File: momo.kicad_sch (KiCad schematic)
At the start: 97 parts, among them SW1 MX_SW_HS, SW10 MX_SW_HS, SW11 MX_SW_HS, SW12 MX_SW_HS, SW13 MX_SW_HS, SW14 MX_SW_HS, SW15 MX_SW_HS, SW16 MX_SW_HS, SW17 MX_SW_HS, SW18 MX_SW_HS, SW19 MX_SW_HS, SW2 MX_SW_HS, SW20 MX_SW_HS, SW21 MX_SW_HS, SW22 MX_SW_HS, SW23 MX_SW_HS, SW24 MX_SW_HS, SW25 MX_SW_HS, SW26 MX_SW_HS, SW27 MX_SW_HS, SW28 MX_SW_HS, SW29 MX_SW_HS, SW3 MX_SW_HS, SW30 MX_SW_HS, SW31 MX_SW_HS, SW32 MX_SW_HS, SW33 MX_SW_HS, SW34 MX_SW_HS, SW35 MX_SW_HS, SW36 MX_SW_HS, SW37 MX_SW_HS, SW38 MX_SW_HS, SW39 MX_SW_HS, SW4 MX_SW_HS, SW40 MX_SW_HS, SW41 MX_SW_HS, SW42 MX_SW_HS, SW43 MX_SW_HS, SW44 MX_SW_HS, SW45 MX_SW_HS, SW46 MX_SW_HS, SW47 MX_SW_HS, SW48 MX_SW_HS, SW5 MX_SW_HS, SW6 MX_SW_HS, SW7 MX_SW_HS, SW8 MX_SW_HS, SW9 MX_SW_HS, U1 WeAct-RP2040-Pico

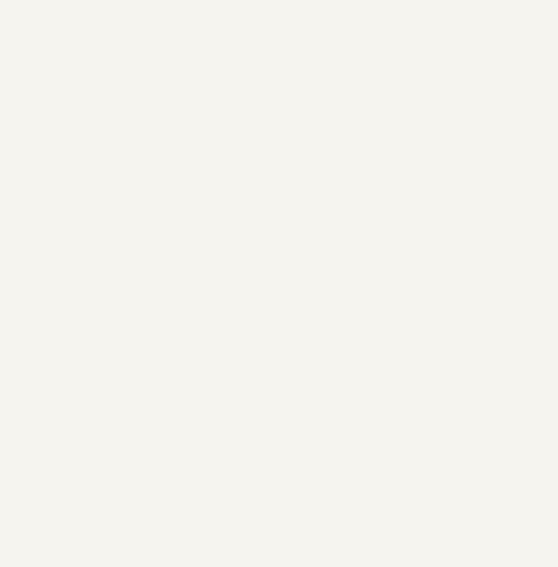
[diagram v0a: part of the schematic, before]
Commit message: Added RGB backlight functionality
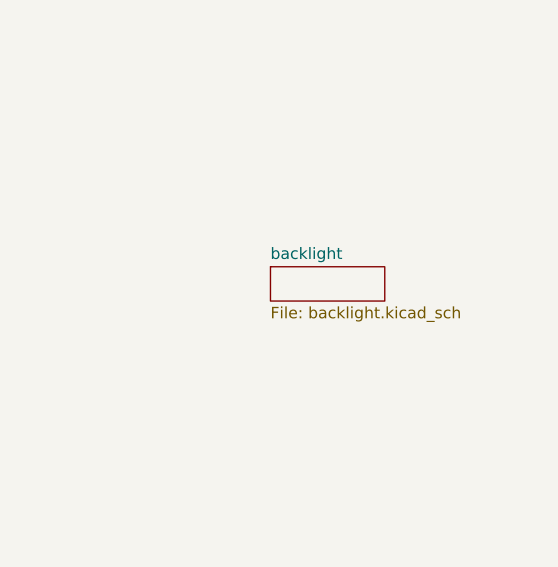
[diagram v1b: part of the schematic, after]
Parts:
- D1, D10, D11, D12, D13, D14, D15, D16, D17, D18, D19, D2, D20, D21, D22, D23, D24, D25, D26, D27, D28, D29, D3, D30, D31, D32, D33, D34, D35, D36, D37, D38, D39, D4, D40, D41, D42, D43, D44, D45, D46, D47, D48, D5, D6, D7, D8, D9: footprint (none) -> keyboard_parts:D_SOD123_axial
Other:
- added sheet backlight (backlight.kicad_sch)

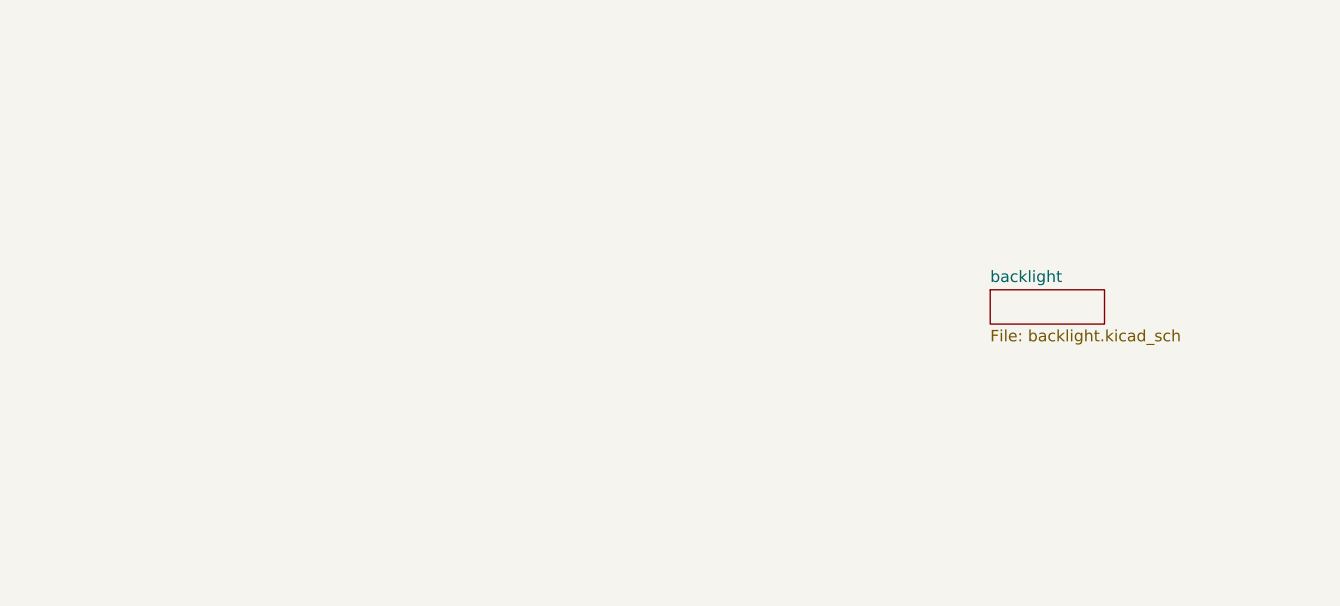
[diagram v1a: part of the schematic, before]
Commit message: Added RGB underglow functionality
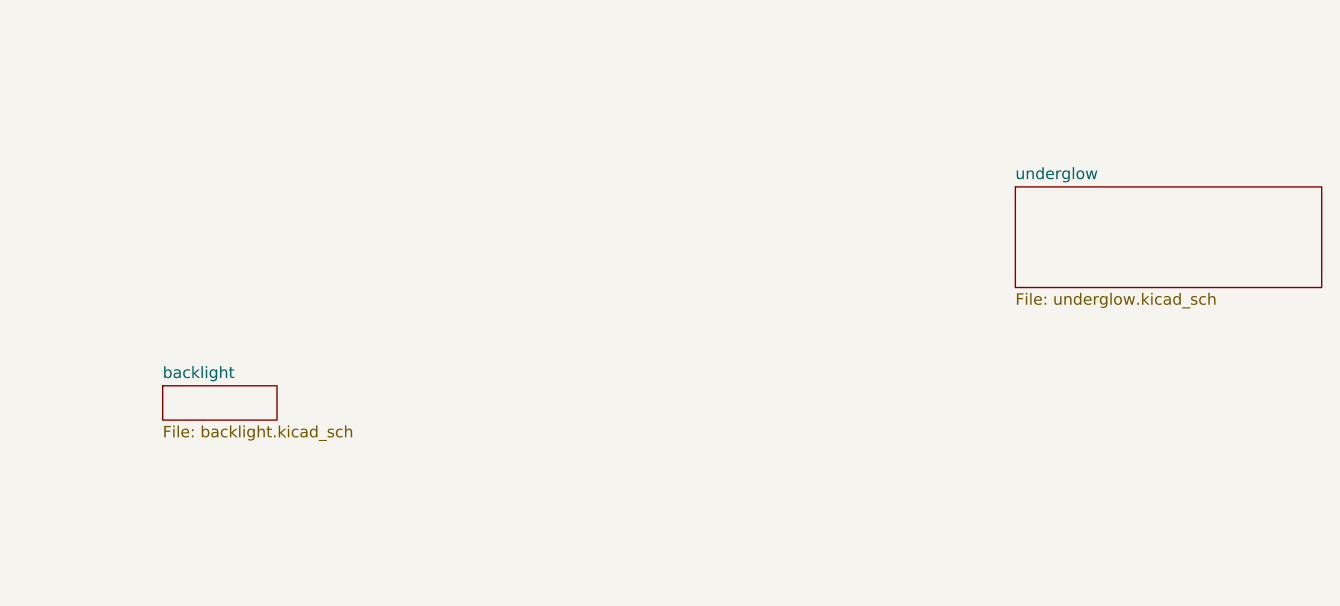
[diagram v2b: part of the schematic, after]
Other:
- added sheet underglow (underglow.kicad_sch)
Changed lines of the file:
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@@
     (pin "9")
   )
-  (sheet (at 311.15 114.3) (size 12.7 3.81) (fields_autoplaced)
+  (sheet (at 219.202 124.968) (size 12.7 3.81) (fields_autoplaced)
     (stroke (width 0.1524) (type solid) (color 0 0 0 0))
     (fill (color 0 0 0 0.0000))
-    (property "Sheet name" "backlight" (id 0) (at 311.15 113.5884 0)
+    (property "Sheet name" "backlight" (id 0) (at 219.202 124.2564 0)
       (effects (font (size 1.27 1.27)) (justify left bottom))
     )
-    (property "Sheet file" "backlight.kicad_sch" (id 1) (at 311.15 118.6946 0)
+    (property "Sheet file" "backlight.kicad_sch" (id 1) (at 219.202 129.3626 0)
+      (effects (font (size 1.27 1.27)) (justify left top))
+    )
+  )
+  (sheet (at 313.944 102.87) (size 34.036 11.176) (fields_autoplaced)
+    (stroke (width 0.1524) (type solid) (color 0 0 0 0))
+    (fill (color 0 0 0 0.0000))
+    (property "Sheet name" "underglow" (id 0) (at 313.944 102.1584 0)
+      (effects (font (size 1.27 1.27)) (justify left bottom))
+    )
+    (property "Sheet file" "underglow.kicad_sch" (id 1) (at 313.944 114.6306 0)
       (effects (font (size 1.27 1.27)) (justify left top))
     )
@@
     (path "/" (page "1"))
     (path "/9d24d119-5b7b-4dd6-a77e-8432ed719570" (page "2"))
+    (path "/e99cffce-74a9-4be0-80a2-98bb8f0554b7" (page "3"))
   )
   (symbol_instances
@@
       (reference "#PWR054") (unit 1) (value "GND") (footprint "")
     )
+    (path "/e99cffce-74a9-4be0-80a2-98bb8f0554b7/1af3a3ca-3065-4f35-8f4b-531eea546ad6"
+      (reference "#PWR?") (unit 1) (value "VCC") (footprint "")
+    )
+    (path "/e99cffce-74a9-4be0-80a2-98bb8f0554b7/255bcbfd-1fd3-4c57-852c-073117da9470"
+      (reference "#PWR?") (unit 1) (value "VCC") (footprint "")
+    )
+    (path "/e99cffce-74a9-4be0-80a2-98bb8f0554b7/286c519f-e218-4927-92ca-c6648bc9f5d4"
+      (reference "#PWR?") (unit 1) (value "GND") (footprint "")
+    )
+    (path "/e99cffce-74a9-4be0-80a2-98bb8f0554b7/33a2550f-d245-4f02-b01e-f1089cd2cb34"
+      (reference "#PWR?") (unit 1) (value "VCC") (footprint "")
+    )
+    (path "/e99cffce-74a9-4be0-80a2-98bb8f0554b7/33e3d1bd-c09b-499f-b8c0-71441a674e76"
+      (reference "#PWR?") (unit 1) (value "VCC") (footprint "")
+    )
+    (path "/e99cffce-74a9-4be0-80a2-98bb8f0554b7/385bfec2-21a7-4a18-8691-a085658c8c89"
+      (reference "#PWR?") (unit 1) (value "VCC") (footprint "")
+    )
+    (path "/e99cffce-74a9-4be0-80a2-98bb8f0554b7/3a7e117d-9009-4a92-9ae7-3cf95631112e"
+      (reference "#PWR?") (unit 1) (value "GND") (footprint "")
+    )
+    (path "/e99cffce-74a9-4be0-80a2-98bb8f0554b7/3c217400-aed6-4acf-baff-9668b9028e4b"
+      (reference "#PWR?") (unit 1) (value "GND") (footprint "")
+    )
+    (path "/e99cffce-74a9-4be0-80a2-98bb8f0554b7/62fb68a9-3c67-4fad-b4d3-634e314d79bf"
+      (reference "#PWR?") (unit 1) (value "GND") (footprint "")
+    )
+    (path "/e99cffce-74a9-4be0-80a2-98bb8f0554b7/69a943d2-1d0b-496f-aca7-fc0dc1ca3e16"
+      (reference "#PWR?") (unit 1) (value "GND") (footprint "")
+    )
+    (path "/e99cffce-74a9-4be0-80a2-98bb8f0554b7/7f8e8ff6-c975-4254-a2c8-bf0f49491244"
+      (reference "#PWR?") (unit 1) (value "GND") (footprint "")
+    )
+    (path "/e99cffce-74a9-4be0-80a2-98bb8f0554b7/8433c9fe-1841-4b4e-be0a-2f042f79798d"
+      (reference "#PWR?") (unit 1) (value "VCC") (footprint "")
+    )
+    (path "/e99cffce-74a9-4be0-80a2-98bb8f0554b7/84b65d91-59f9-435a-bb3c-18beb66e7de1"
+      (reference "#PWR?") (unit 1) (value "GND") (footprint "")
+    )
+    (path "/e99cffce-74a9-4be0-80a2-98bb8f0554b7/85c0819e-bd9a-43dd-8d40-a49c2e72ec3b"
+      (reference "#PWR?") (unit 1) (value "GND") (footprint "")
+    )
+    (path "/e99cffce-74a9-4be0-80a2-98bb8f0554b7/a5c5ebd3-0b2f-4c58-84b9-0acfd348a118"
+      (reference "#PWR?") (unit 1) (value "GND") (footprint "")
+    )
+    (path "/e99cffce-74a9-4be0-80a2-98bb8f0554b7/ad0e55c2-0086-4729-b601-c79b38a60ec5"
+      (reference "#PWR?") (unit 1) (value "GND") (footprint "")
+    )
+    (path "/e99cffce-74a9-4be0-80a2-98bb8f0554b7/b8422dfe-11cc-4720-90cc-62891e1c4a62"
+      (reference "#PWR?") (unit 1) (value "GND") (footprint "")
+    )
+    (path "/e99cffce-74a9-4be0-80a2-98bb8f0554b7/bd320a57-7248-4c21-b7f6-98764999cbae"
+      (reference "#PWR?") (unit 1) (value "GND") (footprint "")
+    )
+    (path "/e99cffce-74a9-4be0-80a2-98bb8f0554b7/bf394f36-d4bd-4c48-83cd-899b4e2bc1ba"
+      (reference "#PWR?") (unit 1) (value "GND") (footprint "")
+    )
+    (path "/e99cffce-74a9-4be0-80a2-98bb8f0554b7/c5b7428d-8a0f-482b-a99e-85b36fb5826c"
+      (reference "#PWR?") (unit 1) (value "GND") (footprint "")
+    )
+    (path "/e99cffce-74a9-4be0-80a2-98bb8f0554b7/c85b58f8-416f-4f1b-91bd-a4a7cfa79558"
+      (reference "#PWR?") (unit 1) (value "VCC") (footprint "")
+    )
+    (path "/e99cffce-74a9-4be0-80a2-98bb8f0554b7/c9a7544f-1c4b-4eb6-88f4-be21a124fd15"
+      (reference "#PWR?") (unit 1) (value "GND") (footprint "")
+    )
+    (path "/e99cffce-74a9-4be0-80a2-98bb8f0554b7/cb6637d4-44d5-4944-b496-4c3eea75e5c7"
+      (reference "#PWR?") (unit 1) (value "GND") (footprint "")
+    )
+    (path "/e99cffce-74a9-4be0-80a2-98bb8f0554b7/ce932e5f-4427-4ec0-baff-044c4be2c049"
+      (reference "#PWR?") (unit 1) (value "GND") (footprint "")
+    )
+    (path "/e99cffce-74a9-4be0-80a2-98bb8f0554b7/dd96ff4a-8d8f-4ac8-b504-9f7312976f18"
+      (reference "#PWR?") (unit 1) (value "VCC") (footprint "")
+    )
+    (path "/e99cffce-74a9-4be0-80a2-98bb8f0554b7/f588f64b-4bb8-4ff9-9273-09d0e82241d3"
+      (reference "#PWR?") (unit 1) (value "VCC") (footprint "")
+    )
+    (path "/e99cffce-74a9-4be0-80a2-98bb8f0554b7/f742018d-9f30-4949-9554-c1972d484680"
+      (reference "#PWR?") (unit 1) (value "GND") (footprint "")
+    )
+    (path "/e99cffce-74a9-4be0-80a2-98bb8f0554b7/1f77dfa0-68fe-4eab-a7e6-8b268254b2e2"
+      (reference "C?") (unit 1) (value "100nF") (footprint "")
+    )
+    (path "/e99cffce-74a9-4be0-80a2-98bb8f0554b7/34a005e4-caf6-481e-a3ae-a697755c709e"
+      (reference "C?") (unit 1) (value "100nF") (footprint "")
+    )
+    (path "/e99cffce-74a9-4be0-80a2-98bb8f0554b7/41b0034d-bea4-4b4f-b3fd-c936d300cb20"
+      (reference "C?") (unit 1) (value "100nF") (footprint "")
+    )
+    (path "/e99cffce-74a9-4be0-80a2-98bb8f0554b7/4d305704-5eae-4101-aac5-78a2259dc56a"
+      (reference "C?") (unit 1) (value "100nF") (footprint "")
+    )
+    (path "/e99cffce-74a9-4be0-80a2-98bb8f0554b7/61c1e6b9-122c-4f60-b157-21366855226b"
+      (reference "C?") (unit 1) (value "100nF") (footprint "")
+    )
+    (path "/e99cffce-74a9-4be0-80a2-98bb8f0554b7/81b3bbc6-d123-4720-b590-1dca10823d8f"
+      (reference "C?") (unit 1) (value "100nF") (footprint "")
+    )
+    (path "/e99cffce-74a9-4be0-80a2-98bb8f0554b7/82c29893-183e-4901-aea1-8f8088dae102"
+      (reference "C?") (unit 1) (value "100nF") (footprint "")
+    )
+    (path "/e99cffce-74a9-4be0-80a2-98bb8f0554b7/b1685cba-e2f4-4828-9f72-2449af376b04"
+      (reference "C?") (unit 1) (value "100nF") (footprint "")
+    )
+    (path "/e99cffce-74a9-4be0-80a2-98bb8f0554b7/d186caea-5c4f-4ab1-82c3-c62a97c042b6"
+      (reference "C?") (unit 1) (value "100nF") (footprint "")
+    )
     (path "/20f0ef94-b4c4-4b36-98fb-027bc3e36c3a"
       (reference "D1") (unit 1) (value "D") (footprint "keyboard_parts:D_SOD123_axial")
@@
       (reference "D48") (unit 1) (value "D") (footprint "keyboard_parts:D_SOD123_axial")
     )
+    (path "/e99cffce-74a9-4be0-80a2-98bb8f0554b7/190153f1-3974-4962-8b8e-3a42765030e9"
+      (reference "D?") (unit 1) (value "WS2812B") (footprint "LED_SMD:LED_WS2812B_PLCC4_5.0x5.0mm_P3.2mm")
+    )
+    (path "/e99cffce-74a9-4be0-80a2-98bb8f0554b7/5d168fa5-7032-4356-a8d7-57bdac2736f3"
+      (reference "D?") (unit 1) (value "WS2812B") (footprint "LED_SMD:LED_WS2812B_PLCC4_5.0x5.0mm_P3.2mm")
+    )
+    (path "/e99cffce-74a9-4be0-80a2-98bb8f0554b7/7336bc54-dc4f-4d46-b191-84d1f5fe07cc"
+      (reference "D?") (unit 1) (value "WS2812B") (footprint "LED_SMD:LED_WS2812B_PLCC4_5.0x5.0mm_P3.2mm")
+    )
+    (path "/e99cffce-74a9-4be0-80a2-98bb8f0554b7/7ac88f28-58d8-4b75-8491-4f4b7ebd7fbb"
+      (reference "D?") (unit 1) (value "WS2812B") (footprint "LED_SMD:LED_WS2812B_PLCC4_5.0x5.0mm_P3.2mm")
+    )
+    (path "/e99cffce-74a9-4be0-80a2-98bb8f0554b7/871128dc-41e5-4680-8e65-92730553ea0a"
+      (reference "D?") (unit 1) (value "WS2812B") (footprint "LED_SMD:LED_WS2812B_PLCC4_5.0x5.0mm_P3.2mm")
+    )
+    (path "/e99cffce-74a9-4be0-80a2-98bb8f0554b7/8a2d8035-9ae7-48ce-ba57-22459a90871a"
+      (reference "D?") (unit 1) (value "WS2812B") (footprint "LED_SMD:LED_WS2812B_PLCC4_5.0x5.0mm_P3.2mm")
+    )
+    (path "/e99cffce-74a9-4be0-80a2-98bb8f0554b7/d10f1286-b2cc-43b1-ae16-0a968db05143"
+      (reference "D?") (unit 1) (value "WS2812B") (footprint "LED_SMD:LED_WS2812B_PLCC4_5.0x5.0mm_P3.2mm")
+    )
+    (path "/e99cffce-74a9-4be0-80a2-98bb8f0554b7/d943b702-005b-491a-9279-c29918a9a347"
+      (reference "D?") (unit 1) (value "WS2812B") (footprint "LED_SMD:LED_WS2812B_PLCC4_5.0x5.0mm_P3.2mm")
+    )
+    (path "/e99cffce-74a9-4be0-80a2-98bb8f0554b7/fa8f5d74-936f-4e3e-85f9-a6b1791545a3"
+      (reference "D?") (unit 1) (value "WS2812B") (footprint "LED_SMD:LED_WS2812B_PLCC4_5.0x5.0mm_P3.2mm")
+    )
     (path "/9d24d119-5b7b-4dd6-a77e-8432ed719570/dd3f1b39-f22c-4b69-9ea9-51559b2d0569"

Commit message: Pin wiring
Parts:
- added J1: USB C, Connector_PinHeader_2.54mm:PinHeader_1x04_P2.54mm_Vertical, symbol Connector:Conn_01x04_Female
- renumbered D37 to D10, D41 to D11, D45 to D12, D2 to D13, D6 to D14, D10 to D15, D14 to D16, D18 to D17, D22 to D18, D26 to D19, D5 to D2, D30 to D20, D34 to D21, D38 to D22, D42 to D23, D46 to D24, D3 to D25, D7 to D26, D11 to D27, D15 to D28, D19 to D29, D9 to D3, D23 to D30, D27 to D31, D31 to D32, D35 to D33, D39 to D34, D43 to D35, D47 to D36, D4 to D37, D8 to D38, D12 to D39, D13 to D4, D16 to D40, D20 to D41, D24 to D42, D28 to D43, D32 to D44, D36 to D45, D40 to D46, D44 to D47, D17 to D5, D21 to D6, D25 to D7, D29 to D8, D33 to D9, SW37 to SW10, SW41 to SW11, SW45 to SW12, SW2 to SW13, SW6 to SW14, SW10 to SW15, SW14 to SW16, SW18 to SW17, SW22 to SW18, SW26 to SW19, SW5 to SW2, SW30 to SW20, SW34 to SW21, SW38 to SW22, SW42 to SW23, SW46 to SW24, SW3 to SW25, SW7 to SW26, SW11 to SW27, SW15 to SW28, SW19 to SW29, SW9 to SW3, SW23 to SW30, SW27 to SW31, SW31 to SW32, SW35 to SW33, SW39 to SW34, SW43 to SW35, SW47 to SW36, SW4 to SW37, SW8 to SW38, SW12 to SW39, SW13 to SW4, SW16 to SW40, SW20 to SW41, SW24 to SW42, SW28 to SW43, SW32 to SW44, SW36 to SW45, SW40 to SW46, SW44 to SW47, SW17 to SW5, SW21 to SW6, SW25 to SW7, SW29 to SW8, SW33 to SW9
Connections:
- net UNDERGLOW: now reaches U1.36 (GP24)
- new net D+: J1.3 (Pin_3)
- new net D-: J1.2 (Pin_2)
- new net GND: J1.4 (Pin_4)
- new net VCC: J1.1 (Pin_1)
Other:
- note added: "I'll use a board which have a WS2812 on pin 23."
